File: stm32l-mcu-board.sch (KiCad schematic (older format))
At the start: 59 parts, among them J1 CON_USB_GCT_USB4105_REVA, J2 PROG, J3 PORT, J4 PORT, Q1 MIC94052YC6-TR, SW1 SW_Push, SW2 SW_Push, U1 IC-SENSOR-TEMP-HUM-SHT4X, U2 W25Q16JVSNIQ, U3 STM32L151CCTx, U4 ADXL343, U5 MCP9701T-E/TT, U6 CH340C, U7 TC1264-3.3VDBTR, Y1 16MHz

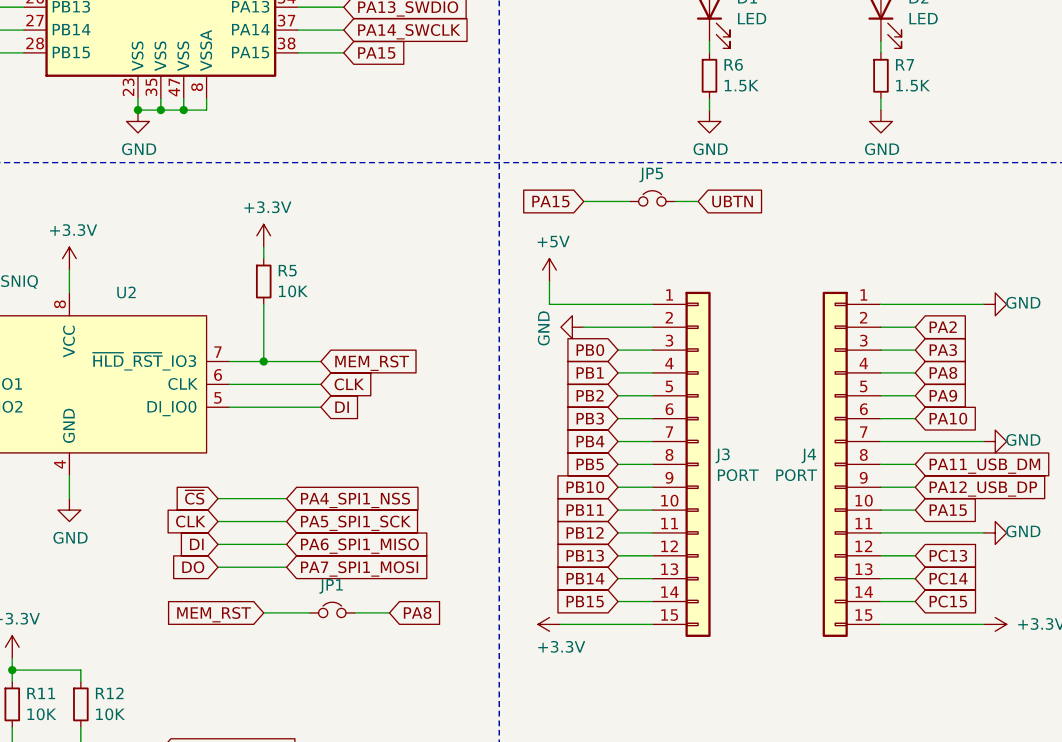
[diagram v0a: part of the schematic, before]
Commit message: Update the Flash memory circuit
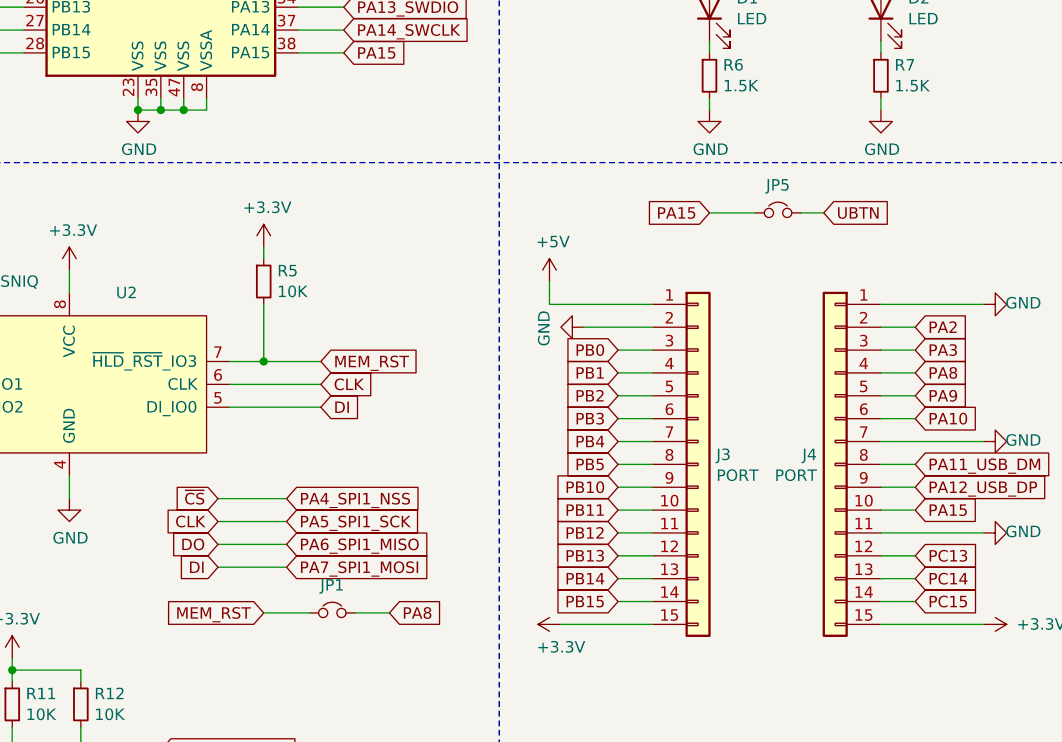
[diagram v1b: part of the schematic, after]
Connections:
- net DI: now also U3.17 (PA7); no longer U3.16 (PA6)
- net DO: now also U3.16 (PA6); no longer U3.17 (PA7)
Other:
- moved on the sheet: JP5
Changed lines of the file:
@@
 Text GLabel 3100 5800 0    50   Input ~ 0
 ~CS
+Text GLabel 3100 6000 0    50   Input ~ 0
+DO
 Text GLabel 3100 6100 0    50   Input ~ 0
-DO
-Text GLabel 3100 6000 0    50   Input ~ 0
 DI
 Text GLabel 3550 5300 2    50   Input ~ 0
@@
 Wire Wire Line
 	3100 5900 3400 5900
-Wire Wire Line
-	3100 6000 3400 6000
-Wire Wire Line
-	3100 6100 3400 6100
 Text GLabel 3300 6300 0    50   Input ~ 0
 MEM_RST
@@
 	1    0    0    -1
 $EndComp
-Text GLabel 5200 4500 2    50   Input ~ 0
+Text GLabel 5750 4550 2    50   Input ~ 0
 UBTN
 $Comp
 L Device:Jumper_NC_Small JP5
 U 1 1 62864A8F
-P 5000 4500
-F 0 "JP5" H 5000 4621 50  0000 C CNN
-F 1 "Jumper_NC_Small" H 5000 4621 50  0001 C CNN
-F 2 "Jumper:SolderJumper-2_P1.3mm_Open_RoundedPad1.0x1.5mm" H 5000 4500 50  0001 C CNN
-F 3 "~" H 5000 4500 50  0001 C CNN
-	1    5000 4500
-	1    0    0    -1
-$EndComp
-Text GLabel 4700 4500 0    50   Input ~ 0
+P 5550 4550
+F 0 "JP5" H 5550 4671 50  0000 C CNN
+F 1 "Jumper_NC_Small" H 5550 4671 50  0001 C CNN
+F 2 "Jumper:SolderJumper-2_P1.3mm_Open_RoundedPad1.0x1.5mm" H 5550 4550 50  0001 C CNN
+F 3 "~" H 5550 4550 50  0001 C CNN
+	1    5550 4550
+	1    0    0    -1
+$EndComp
+Text GLabel 5250 4550 0    50   Input ~ 0
 PA15
 Wire Wire Line
-	4700 4500 4900 4500
-Wire Wire Line
-	5100 4500 5200 4500
+	5250 4550 5450 4550
+Wire Wire Line
+	5650 4550 5750 4550
 $Comp
 L power:GND #PWR051
@@
 	8900 4850 9750 4850
 NoConn ~ 9350 5250
+Wire Wire Line
+	3100 6000 3400 6000
+Wire Wire Line
+	3100 6100 3400 6100
 $EndSCHEMATC
